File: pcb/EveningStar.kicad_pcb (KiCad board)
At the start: 2 copper layers, 107 x 97.2 mm, 153 parts, among them J2 DEBUG, P1 WJ15EDGRC-3.81-2P, Q1 2N7002, U1 78L05G, U11 15uH, U3 ISO6721RBDR, U5 74HC14D, U6 LMR38020SDDAR, U7 ESP32-C6-WROOM-1-N8, U8 GD5F2GM7UEYIGR, U9 W5500, X1 32.768kHz, Y1 25MHz

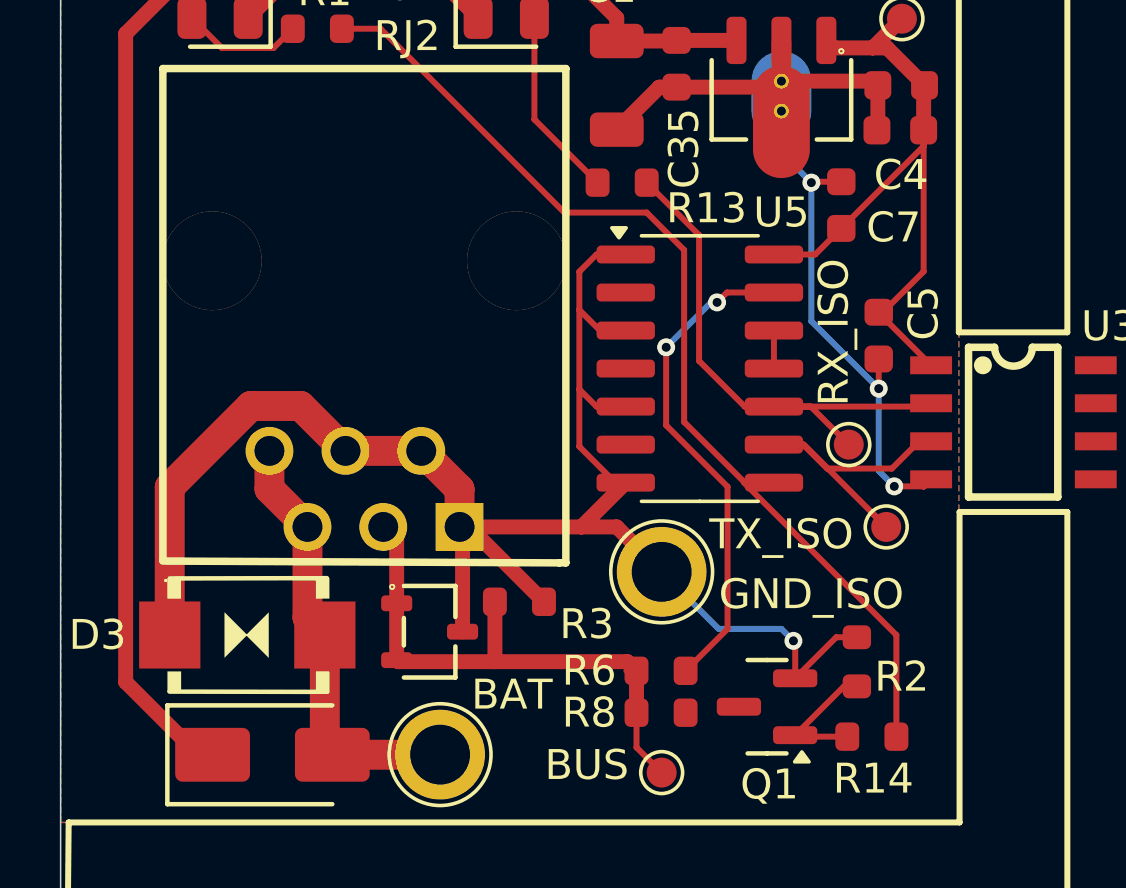
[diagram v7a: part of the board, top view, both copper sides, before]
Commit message: pcb(mb_frontend): clean up silkscreen labels
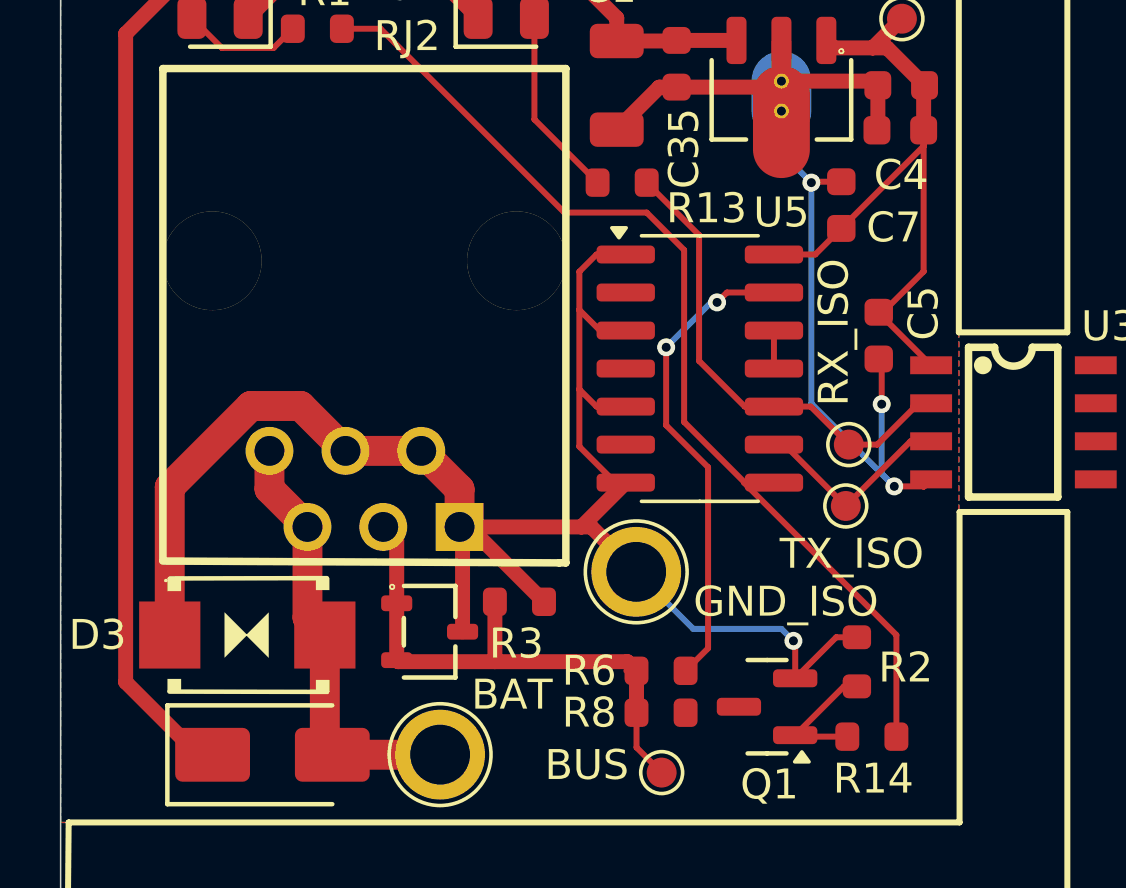
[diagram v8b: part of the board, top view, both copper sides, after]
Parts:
- moved TP27 1.52 mm to (64.6, 65.6)
- moved TP25 0.85 mm to (57.6, 67.8)
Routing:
- net /meterbus_frontend/WRITE_ISO: track 11.7 -> 7.15 mm
- net GND_ISO: track 96.2 -> 98.2 mm
- net /meterbus_frontend/READ_ISO: track 18.3 -> 16.5 mm
- net Net-(R6-Pad2): track 16.6 -> 16.1 mm
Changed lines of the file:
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@@
 		(tags "resistor")
 		(property "Reference" "R3"
-			(at 2.25 0.75 0)
+			(at -0.1 1.4 0)
 			(layer "F.SilkS")
 			(effects
@@
 	(footprint "TestPoint:TestPoint_Plated_Hole_D2.0mm"
 		(layer "F.Cu")
-		(at 58.45 67.8)
+		(at 57.6 67.8)
 		(descr "Plated Hole as test Point, diameter 2.0mm")
 		(tags "test point plated hole")
@@
 		)
 		(property "Value" "GND_ISO"
-			(at 5 0.75 0)
+			(at 5 1 0)
 			(layer "F.SilkS")
 			(effects
@@
 		(sheetname "/meterbus_frontend/")
 		(sheetfile "meterbus_frontend.kicad_sch")
-		(units
-			(unit
-				(name "A")
-				(pins "1" "2")
-			)
-		)
 		(attr through_hole)
 		(duplicate_pad_numbers_are_jumpers no)
@@
 		(fp_poly
 			(pts
-				(xy -0.045009 0.003759) (xy 0.716991 0.765759) (xy 0.716991 -0.758241) (xy -0.045009 0.003759)
+				(xy -2.667 -1.905) (xy -2.667 -1.465492) (xy -2.2098 -1.465492) (xy -2.2098 -1.905)
 			)
 			(stroke
@@
 		(fp_poly
 			(pts
-				(xy 0 0) (xy -0.762 -0.762) (xy -0.762 0.762) (xy 0 0)
+				(xy -2.667 1.905) (xy -2.667 1.465492) (xy -2.2098 1.465492) (xy -2.2098 1.905)
 			)
 			(stroke
@@
 		(fp_poly
 			(pts
-				(xy -2.667 -1.905) (xy -2.667 -1.215492) (xy -2.2098 -1.215492) (xy -2.2098 -1.905) (xy -2.667 -1.905)
+				(xy -0.045009 0.003759) (xy 0.716991 0.765759) (xy 0.716991 -0.758241) (xy -0.045009 0.003759)
 			)
 			(stroke
@@
 		(fp_poly
 			(pts
-				(xy -2.667 1.905) (xy -2.667 1.215492) (xy -2.2098 1.215492) (xy -2.2098 1.905) (xy -2.667 1.905)
+				(xy 0 0) (xy -0.762 -0.762) (xy -0.762 0.762) (xy 0 0)
 			)
 			(stroke
@@
 		(fp_poly
 			(pts
-				(xy 2.286 -1.905) (xy 2.286 -1.215492) (xy 2.7432 -1.215492) (xy 2.7432 -1.905) (xy 2.286 -1.905)
+				(xy 2.286 -1.905) (xy 2.286 -1.5) (xy 2.7432 -1.5) (xy 2.7432 -1.905)
 			)
 			(stroke
@@
 		(fp_poly
 			(pts
-				(xy 2.286 1.905) (xy 2.286 1.215492) (xy 2.7432 1.215492) (xy 2.7432 1.905) (xy 2.286 1.905)
+				(xy 2.286 1.905) (xy 2.286 1.5) (xy 2.7432 1.5) (xy 2.7432 1.905)
 			)
 			(stroke
@@
 		(tags "resistor")
 		(property "Reference" "R2"
-			(at -0.5 1.5 180)
+			(at -0.195 1.63 180)
 			(layer "F.SilkS")
 			(effects
@@
 	(footprint "TestPoint:TestPoint_Pad_D1.0mm"
 		(layer "F.Cu")
-		(at 65.95 66.3)
+		(at 64.6 65.6)
 		(descr "SMD pad as test Point, diameter 1.0mm")
 		(tags "test point SMD pad")
@@
 		)
 		(property "Value" "TX_ISO"
-			(at -3.5 0.25 0)
+			(at 0.2 1.6 180)
 			(layer "F.SilkS")
 			(effects
@@
 	)
 	(segment
+		(start 56.1 66.3)
+		(end 57.6 67.8)
+		(width 0.5)
+		(layer "F.Cu")
+		(net "GND_ISO")
+	)
+	(segment
 		(start 65.67 51.55)
 		(end 65.67 53.02)
@@
 	)
 	(segment
-		(start 56.95 66.3)
-		(end 58.45 67.8)
-		(width 0.5)
+		(start 56.275001 57.2)
+		(end 55.7 57.775001)
+		(width 0.2)
 		(layer "F.Cu")
 		(net "GND_ISO")
 	)
 	(segment
-		(start 56.275001 57.2)
-		(end 55.7 57.775001)
+		(start 65.8 62.2)
+		(end 65.8 60.79)
 		(width 0.2)
 		(layer "F.Cu")
@@
 	)
 	(segment
-		(start 65.7 60.83)
-		(end 65.7 61.68)
-		(width 0.2)
-		(layer "F.Cu")
-		(net "GND_ISO")
-	)
-	(segment
 		(start 51.8 66.4)
 		(end 51.7 66.3)
@@
 	)
 	(segment
+		(start 65.8 60.79)
+		(end 65.7 60.69)
+		(width 0.2)
+		(layer "F.Cu")
+		(net "GND_ISO")
+	)
+	(segment
 		(start 56.904448 64.82)
 		(end 57.25 64.82)
@@
 	(segment
 		(start 55.77 66.3)
-		(end 57.25 64.82)
+		(end 56.1 66.3)
 		(width 0.5)
 		(layer "F.Cu")
@@
 	(segment
 		(start 55.77 66.3)
-		(end 56.95 66.3)
+		(end 57.25 64.82)
 		(width 0.5)
 		(layer "F.Cu")
@@
 	)
 	(via
-		(at 65.7 61.68)
+		(at 65.8 62.2)
 		(size 0.6)
 		(drill 0.3)
@@
 	)
 	(segment
-		(start 60.355 69.705)
-		(end 58.45 67.8)
+		(start 65.8 62.2)
+		(end 65.8 64.525439)
 		(width 0.2)
 		(layer "B.Cu")
@@
 	)
 	(segment
-		(start 62.45 53.8)
-		(end 63.45 54.8)
+		(start 59.505 69.705)
+		(end 57.6 67.8)
 		(width 0.2)
 		(layer "B.Cu")
@@
 	)
 	(segment
-		(start 58.56 67.16)
-		(end 59.7 68.3)
+		(start 62.45 53.8)
+		(end 63.45 54.8)
 		(width 0.2)
 		(layer "B.Cu")
@@
 	(segment
 		(start 62.45 69.705)
-		(end 60.355 69.705)
-		(width 0.2)
-		(layer "B.Cu")
-		(net "GND_ISO")
-	)
-	(segment
-		(start 65.7 61.68)
-		(end 65.7 64.425439)
+		(end 59.505 69.705)
 		(width 0.2)
 		(layer "B.Cu")
@@
 	)
 	(segment
-		(start 63.45 59.43)
-		(end 65.7 61.68)
+		(start 65.8 64.525439)
+		(end 66.219298 64.944737)
 		(width 0.2)
 		(layer "B.Cu")
@@
 	)
 	(segment
-		(start 63.45 54.8)
-		(end 63.45 59.43)
+		(start 66.219298 64.944737)
+		(end 63.45 62.175439)
 		(width 0.2)
 		(layer "B.Cu")
@@
 	)
 	(segment
-		(start 65.7 64.425439)
-		(end 66.219298 64.944737)
+		(start 63.45 62.175439)
+		(end 63.45 54.8)
 		(width 0.2)
 		(layer "B.Cu")
@@
 	)
 	(segment
+		(start 67.45 62.17)
+		(end 67.03 62.17)
+		(width 0.2)
+		(layer "F.Cu")
+		(net "/meterbus_frontend/READ_ISO")
+	)
+	(segment
 		(start 61.225001 62.28)
 		(end 62.2 62.28)
@@
 	)
 	(segment
-		(start 62.2 62.28)
-		(end 67.34 62.28)
+		(start 67.03 62.17)
+		(end 65.65 63.55)
 		(width 0.2)
 		(layer "F.Cu")
@@
 	)
 	(segment
+		(start 65.65 63.55)
+		(end 64.7 63.55)
+		(width 0.2)
+		(layer "F.Cu")
+		(net "/meterbus_frontend/READ_ISO")
+	)
+	(segment
 		(start 57.95 54.8)
 		(end 59.7 56.55)
@@
 	)
 	(segment
-		(start 63.174999 63.55)
-		(end 62.2 63.55)
-		(width 0.2)
-		(layer "F.Cu")
-		(net "/meterbus_frontend/WRITE_ISO")
-	)
-	(segment
-		(start 65.45 65.8)
-		(end 65.95 66.3)
+		(start 67.45 63.44)
+		(end 66.76 63.44)
 		(width 0.2)
 		(layer "F.Cu")
@@
 	)
 	(segment
-		(start 67.45 63.44)
-		(end 67.05 63.44)
+		(start 66.76 63.44)
+		(end 64.6 65.6)
 		(width 0.2)
 		(layer "F.Cu")
@@
 	)
 	(segment
-		(start 62.2 63.55)
-		(end 63.2 63.55)
+		(start 62.55 63.55)
+		(end 62.2 63.55)
 		(width 0.2)
 		(layer "F.Cu")
@@
 	)
 	(segment
-		(start 63.2 63.55)
-		(end 65.95 66.3)
-		(width 0.2)
-		(layer "F.Cu")
-		(net "/meterbus_frontend/WRITE_ISO")
-	)
-	(segment
-		(start 63.974999 64.35)
-		(end 63.174999 63.55)
-		(width 0.2)
-		(layer "F.Cu")
-		(net "/meterbus_frontend/WRITE_ISO")
-	)
-	(segment
-		(start 67.05 63.44)
-		(end 66.14 64.35)
+		(start 64.6 65.6)
+		(end 62.55 63.55)
 		(width 0.2)
 		(layer "F.Cu")
@@
 	)
 	(segment
-		(start 66.14 64.35)
-		(end 63.974999 64.35)
+		(start 62.2 59.74)
+		(end 62.2 61.01)
 		(width 0.2)
 		(layer "F.Cu")
-		(net "/meterbus_frontend/WRITE_ISO")
+		(net "Net-(U5-Pad11)")
 	)
 	(segment
-		(start 62.2 59.74)
-		(end 62.2 61.01)
+		(start 60 70.355)
+		(end 60 64.305)
 		(width 0.2)
 		(layer "F.Cu")
-		(net "Net-(U5-Pad11)")
+		(net "Net-(R6-Pad2)")
 	)
 	(segment
@@
 	)
 	(segment
-		(start 60.65 69.705)
-		(end 60.65 64.955)
+		(start 60 64.305)
+		(end 58.6 62.905)
 		(width 0.2)
 		(layer "F.Cu")
@@
 	(segment
 		(start 59.25 71.105)
-		(end 60.65 69.705)
-		(width 0.2)
-		(layer "F.Cu")
-		(net "Net-(R6-Pad2)")
-	)
-	(segment
-		(start 60.65 64.955)
-		(end 58.6 62.905)
+		(end 60 70.355)
 		(width 0.2)
 		(layer "F.Cu")
